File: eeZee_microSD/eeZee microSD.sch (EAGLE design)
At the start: 12 parts, among them U1 MCP1824S

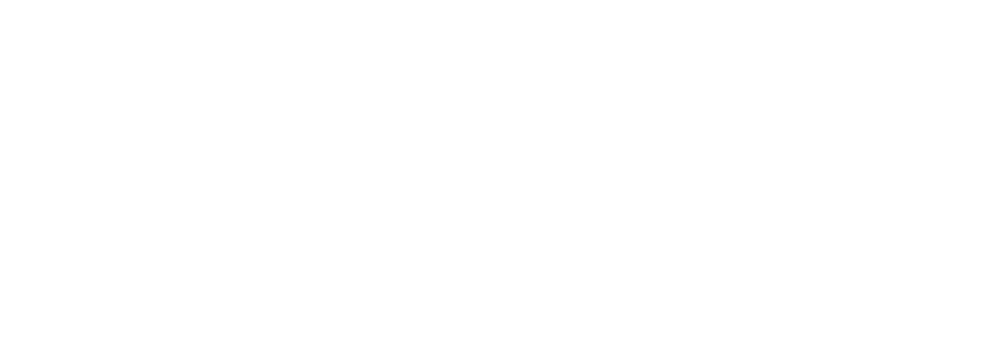
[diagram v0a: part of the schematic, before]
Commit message: Added name/rev
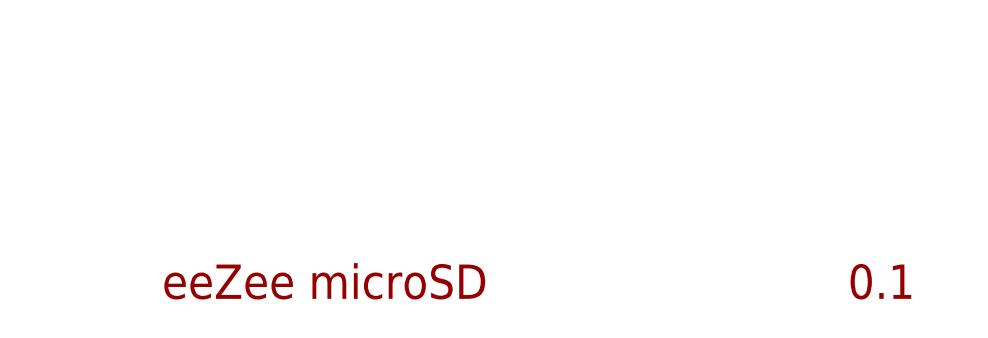
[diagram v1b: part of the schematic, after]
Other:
- note added: "0.1"
- note added: "eeZee microSD"
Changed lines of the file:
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@@
 <grid distance="0.1" unitdist="inch" unit="inch" style="lines" multiple="1" display="no" altdistance="0.01" altunitdist="inch" altunit="inch"/>
 <layers>
-<layer number="1" name="Top" color="4" fill="1" visible="yes" active="no"/>
-<layer number="16" name="Bottom" color="1" fill="1" visible="yes" active="no"/>
-<layer number="17" name="Pads" color="2" fill="1" visible="yes" active="no"/>
-<layer number="18" name="Vias" color="2" fill="1" visible="yes" active="no"/>
-<layer number="19" name="Unrouted" color="6" fill="1" visible="yes" active="no"/>
-<layer number="20" name="Dimension" color="15" fill="1" visible="yes" active="no"/>
-<layer number="21" name="tPlace" color="7" fill="1" visible="yes" active="no"/>
-<layer number="22" name="bPlace" color="7" fill="1" visible="yes" active="no"/>
-<layer number="23" name="tOrigins" color="15" fill="1" visible="yes" active="no"/>
-<layer number="24" name="bOrigins" color="15" fill="1" visible="yes" active="no"/>
-<layer number="25" name="tNames" color="7" fill="1" visible="yes" active="no"/>
-<layer number="26" name="bNames" color="7" fill="1" visible="yes" active="no"/>
-<layer number="27" name="tValues" color="7" fill="1" visible="yes" active="no"/>
-<layer number="28" name="bValues" color="7" fill="1" visible="yes" active="no"/>
+<layer number="1" name="Top" color="4" fill="1" visible="no" active="no"/>
+<layer number="16" name="Bottom" color="1" fill="1" visible="no" active="no"/>
+<layer number="17" name="Pads" color="2" fill="1" visible="no" active="no"/>
+<layer number="18" name="Vias" color="2" fill="1" visible="no" active="no"/>
+<layer number="19" name="Unrouted" color="6" fill="1" visible="no" active="no"/>
+<layer number="20" name="Dimension" color="15" fill="1" visible="no" active="no"/>
+<layer number="21" name="tPlace" color="7" fill="1" visible="no" active="no"/>
+<layer number="22" name="bPlace" color="7" fill="1" visible="no" active="no"/>
+<layer number="23" name="tOrigins" color="15" fill="1" visible="no" active="no"/>
+<layer number="24" name="bOrigins" color="15" fill="1" visible="no" active="no"/>
+<layer number="25" name="tNames" color="7" fill="1" visible="no" active="no"/>
+<layer number="26" name="bNames" color="7" fill="1" visible="no" active="no"/>
+<layer number="27" name="tValues" color="7" fill="1" visible="no" active="no"/>
+<layer number="28" name="bValues" color="7" fill="1" visible="no" active="no"/>
 <layer number="29" name="tStop" color="7" fill="3" visible="no" active="no"/>
 <layer number="30" name="bStop" color="7" fill="6" visible="no" active="no"/>
@@
 <layer number="35" name="tGlue" color="7" fill="4" visible="no" active="no"/>
 <layer number="36" name="bGlue" color="7" fill="5" visible="no" active="no"/>
-<layer number="37" name="tTest" color="7" fill="1" visible="yes" active="no"/>
-<layer number="38" name="bTest" color="7" fill="1" visible="yes" active="no"/>
+<layer number="37" name="tTest" color="7" fill="1" visible="no" active="no"/>
+<layer number="38" name="bTest" color="7" fill="1" visible="no" active="no"/>
 <layer number="39" name="tKeepout" color="4" fill="11" visible="no" active="no"/>
 <layer number="40" name="bKeepout" color="1" fill="11" visible="no" active="no"/>
@@
 <layer number="44" name="Drills" color="7" fill="1" visible="no" active="no"/>
 <layer number="45" name="Holes" color="7" fill="1" visible="no" active="no"/>
-<layer number="46" name="Milling" color="3" fill="1" visible="yes" active="no"/>
-<layer number="47" name="Measures" color="7" fill="1" visible="yes" active="no"/>
-<layer number="48" name="Document" color="7" fill="1" visible="yes" active="no"/>
-<layer number="49" name="Reference" color="7" fill="1" visible="yes" active="no"/>
-<layer number="50" name="dxf" color="7" fill="1" visible="yes" active="no"/>
-<layer number="51" name="tDocu" color="11" fill="1" visible="yes" active="no"/>
-<layer number="52" name="bDocu" color="7" fill="1" visible="yes" active="no"/>
-<layer number="53" name="tGND_GNDA" color="7" fill="9" visible="yes" active="no"/>
-<layer number="54" name="bGND_GNDA" color="1" fill="9" visible="yes" active="no"/>
-<layer number="56" name="wert" color="7" fill="1" visible="yes" active="no"/>
+<layer number="46" name="Milling" color="3" fill="1" visible="no" active="no"/>
+<layer number="47" name="Measures" color="7" fill="1" visible="no" active="no"/>
+<layer number="48" name="Document" color="7" fill="1" visible="no" active="no"/>
+<layer number="49" name="Reference" color="7" fill="1" visible="no" active="no"/>
+<layer number="50" name="dxf" color="7" fill="1" visible="no" active="no"/>
+<layer number="51" name="tDocu" color="11" fill="1" visible="no" active="no"/>
+<layer number="52" name="bDocu" color="7" fill="1" visible="no" active="no"/>
+<layer number="53" name="tGND_GNDA" color="7" fill="9" visible="no" active="no"/>
+<layer number="54" name="bGND_GNDA" color="1" fill="9" visible="no" active="no"/>
+<layer number="56" name="wert" color="7" fill="1" visible="no" active="no"/>
 <layer number="91" name="Nets" color="2" fill="1" visible="yes" active="yes"/>
 <layer number="92" name="Busses" color="1" fill="1" visible="yes" active="yes"/>
@@
 <text x="161.544" y="138.43" size="1.778" layer="97">Note: select to regulate VCC down to 3.3V or</text>
 <text x="161.544" y="135.89" size="1.778" layer="97">to bypass regulator and send VCC direct to the microSD</text>
+<text x="154.94" y="22.86" size="3.81" layer="94">eeZee microSD</text>
+<text x="231.14" y="22.86" size="3.81" layer="94">0.1</text>
 </plain>
 <instances>

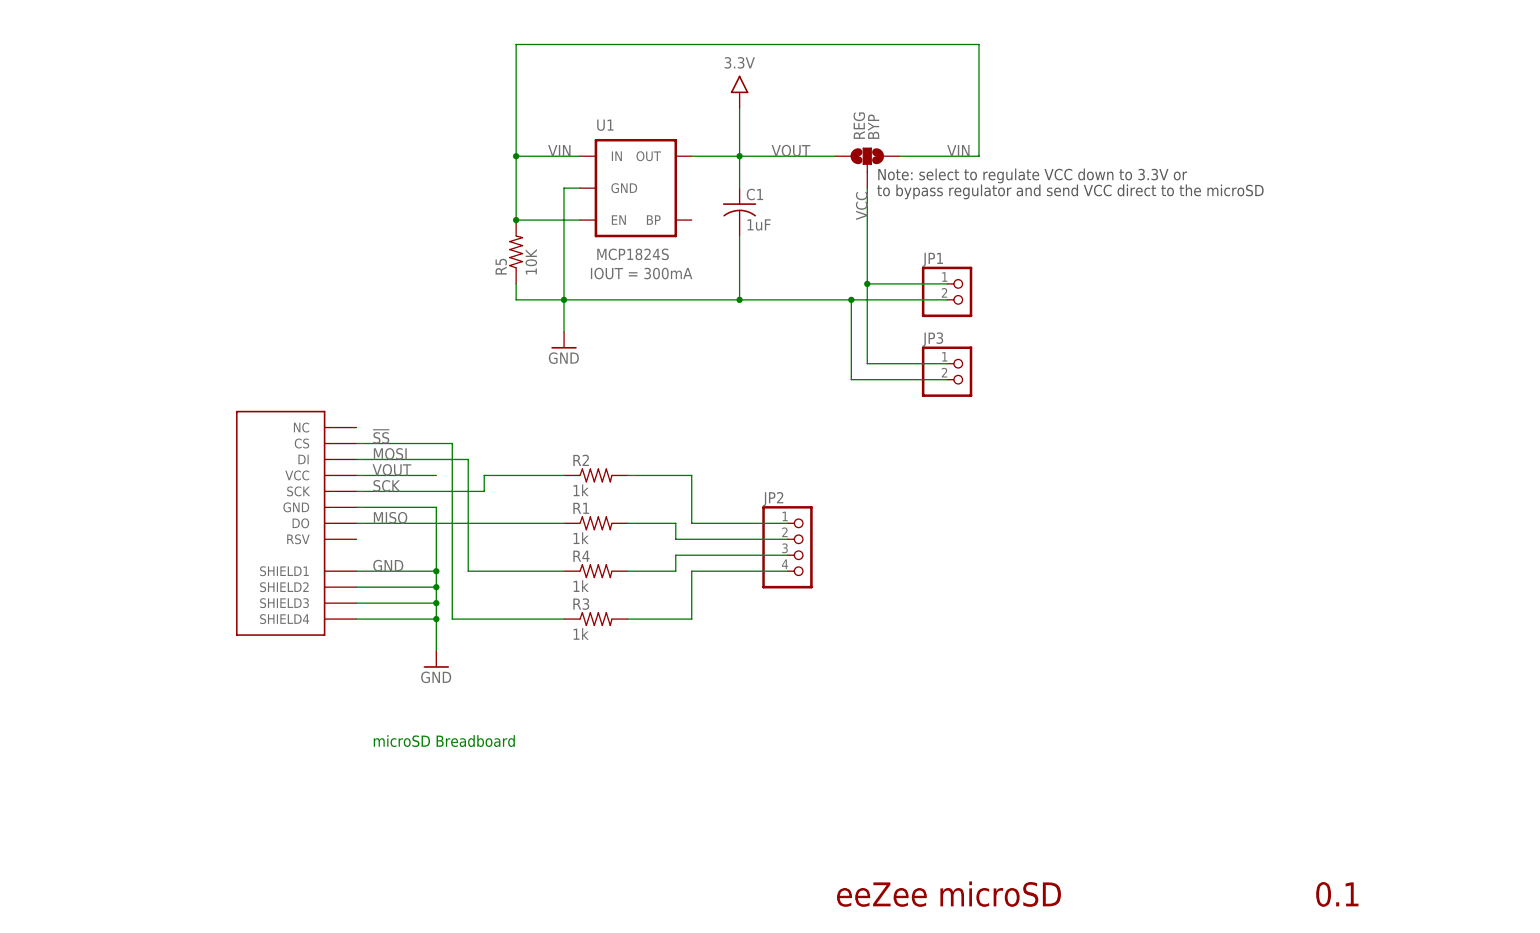
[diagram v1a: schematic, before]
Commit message: Added offset power strip header, tweaked layout, optimized 74HC4050 pin use, etc.
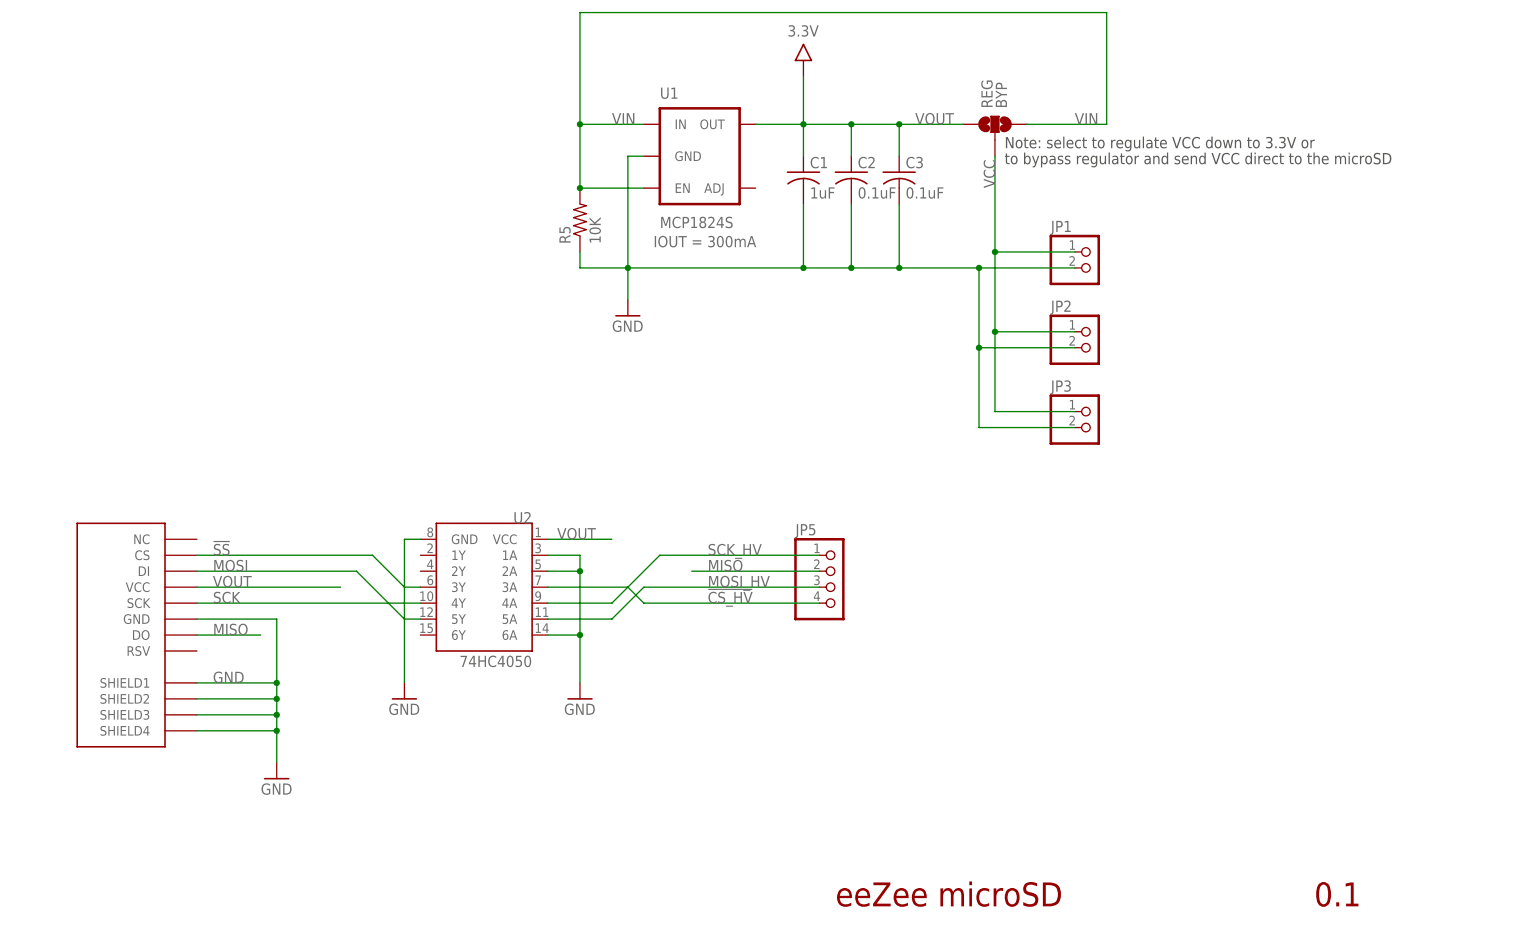
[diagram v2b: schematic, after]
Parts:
- removed R1, R2, R3, R4: 1k, rcl:R-US_R0603
- added C2, C3: 0.1uF, rcl:C-USC0603
- added JP5: (no value), pinhead-2:PINHD-1X04_2.54-S
- added U2: 74HC4050, SparkFun:HEX_CONVERTER
- C1: device rcl:C-USC0805 -> rcl:C-USC0603; PARTNO JMK212BJ226MG-T -> LMK107B7105KA-T
- JP2: device pinhead-2:PINHD-1X04_2.54-S -> pinhead-2:PINHD-1X02_2.54-S
- U1: device SparkFun:V_REG_LDOSMD -> mes_regulators:MCP1824
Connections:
- removed net !SS_HV: JP2.4, R3.2
- removed net MISO_HV: JP2.2, R1.2
- removed net N$2: JP2.3, R4.2
- new net !CS_HV: JP5.4, U2.3A
- new net MOSI_HV: JP5.3, U2.5A
- net !SS: now also U2.3Y; no longer R3.1
- net GND: now also C2.2, C3.2, JP2.2, U2.1A, U2.2A, U2.6A, U2.GND
- net MISO: now also JP5.2; no longer R1.1
- net MOSI: now also U2.5Y; no longer R4.1
- net SCK: now also U2.4Y; no longer R2.1
- net SCK_HV: now also JP5.1, U2.4A; no longer JP2.1, R2.2
- net VCC: now also JP2.1
- net VOUT: now also C2.1, C3.1, U2.VCC
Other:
- note removed: "microSD Breadboard"
- moved on the sheet: C1, JP1, JP3, R5, REG, U1

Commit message: Layout tweaks to fix power pin alignment.
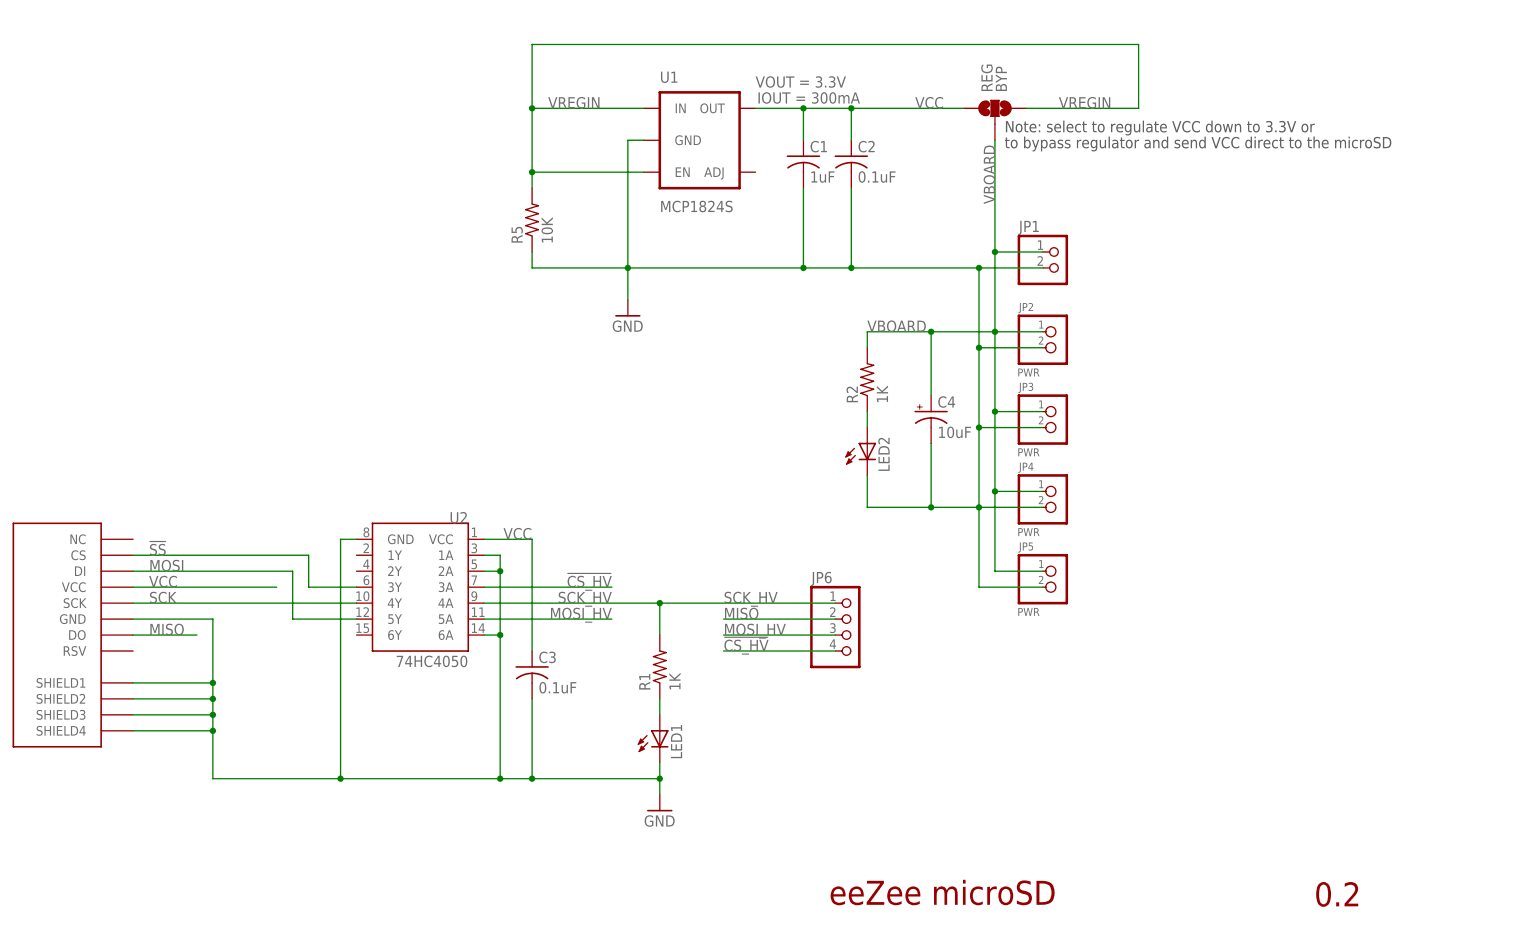
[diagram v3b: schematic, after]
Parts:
- added C4: 10uF, rcl:CPOL-USSMCB
- added JP4: PWR, mes_electromech:PINHEAD-2BIG
- added JP6: (no value), pinhead-2:PINHD-1X04_2.54-S
- added LED1, LED2: (no value), mes_opto:LEDCHIPLED_0805
- added R1, R2: 1K, rcl:R-US_R0603
- JP2, JP3: value (none) -> PWR; device pinhead-2:PINHD-1X02_2.54-S -> mes_electromech:PINHEAD-2BIG
- JP5: value (none) -> PWR; device pinhead-2:PINHD-1X04_2.54-S -> mes_electromech:PINHEAD-2BIG
- U1: VOUT (none) -> 3.3V
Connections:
- net VIN renamed VREGIN
- removed net VOUT: C1.1, C2.1, C3.1, REG.1, U$1.VCC, U1.OUT, U2.VCC
- new net N$1: LED2.A, R2.1
- new net N$2: LED1.A, R1.1
- new net VBOARD: C4.+, JP1.1, JP2.1, JP3.1, JP4.1, JP5.1, R2.2, REG.2
- net !CS_HV: now also JP6.4; no longer JP5.4
- net GND: now also C4.-, JP4.2, JP5.2, LED1.C, LED2.C
- net MISO: now also JP6.2; no longer JP5.2
- net MOSI_HV: now also JP6.3; no longer JP5.3
- net SCK_HV: now also JP6.1, R1.2; no longer JP5.1
- net VCC: now also C1.1, C2.1, C3.1, REG.1, U$1.VCC, U1.OUT, U2.VCC; no longer JP1.1, JP2.1, JP3.1, REG.2
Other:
- note added: "0.2"
- note removed: "0.1"
- moved on the sheet: C1, C2, C3, JP1, R5, REG, U1, U2
